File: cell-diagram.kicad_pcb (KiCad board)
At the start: 2 copper layers, 7 parts, among them Q1 Q_NMOS_GSD, Q2 Q_PMOS_GSD, Q3 Q_NMOS_GSD, Q4 Q_PMOS_GSD, Q5 Q_NMOS_GSD, Q6 Q_NMOS_GSD

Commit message: finish routing
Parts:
- added D1: LED, footprints:LED_1206_ReverseMountSquare1.5mm_HandSolder, B.Cu at (170.2, 96.5)
- added D10: LED, footprints:LED_1206_ReverseMountSquare1.5mm_HandSolder, B.Cu at (157.0, 106.7)
- added D11: LED, footprints:LED_1206_ReverseMountSquare1.5mm_HandSolder, B.Cu at (150.4, 102.1)
- added D12: LED, footprints:LED_1206_ReverseMountSquare1.5mm_HandSolder, B.Cu at (150.4, 113.3)
- added D13: LED, footprints:LED_1206_ReverseMountSquare1.5mm_HandSolder, B.Cu at (129.5, 83.8)
- added D14: LED, footprints:LED_1206_ReverseMountSquare1.5mm_HandSolder, B.Cu at (129.5, 101.6)
- added D15: LED, footprints:LED_1206_ReverseMountSquare1.5mm_HandSolder, B.Cu at (129.5, 119.4)
- added D16: LED, footprints:LED_1206_ReverseMountSquare1.5mm_HandSolder, B.Cu at (175.3, 83.8)
- added D17: LED, footprints:LED_1206_ReverseMountSquare1.5mm_HandSolder, B.Cu at (175.3, 101.6)
- added D18: LED, footprints:LED_1206_ReverseMountSquare1.5mm_HandSolder, B.Cu at (175.3, 119.4)
- added D2: LED, footprints:LED_1206_ReverseMountSquare1.5mm_HandSolder, B.Cu at (160.5, 88.9)
- added D3: LED, footprints:LED_1206_ReverseMountSquare1.5mm_HandSolder, B.Cu at (144.3, 88.9)
- added D4: LED, footprints:LED_1206_ReverseMountSquare1.5mm_HandSolder, B.Cu at (134.6, 96.5)
- added D5: LED, footprints:LED_1206_ReverseMountSquare1.5mm_HandSolder, B.Cu at (154.4, 102.1)
- added D6: LED, footprints:LED_1206_ReverseMountSquare1.5mm_HandSolder, B.Cu at (154.4, 113.3)
- added D7: LED, footprints:LED_1206_ReverseMountSquare1.5mm_HandSolder, B.Cu at (147.8, 108.7)
- added D8: LED, footprints:LED_1206_ReverseMountSquare1.5mm_HandSolder, B.Cu at (140.7, 108.7)
- added D9: LED, footprints:LED_1206_ReverseMountSquare1.5mm_HandSolder, B.Cu at (164.1, 106.7)
- added J1: USB_B_Micro, Connector_USB:USB_Micro-B_Wuerth_629105150521, B.Cu at (167.6, 121.9)
- added Q10: Q_NMOS_GSD, Package_TO_SOT_SMD:SOT-23_Handsoldering, B.Cu at (131.1, 113.8)
- added Q11: Q_NMOS_GSD, Package_TO_SOT_SMD:SOT-23_Handsoldering, B.Cu at (173.7, 113.8)
- added Q7: Q_NMOS_GSD, Package_TO_SOT_SMD:SOT-23_Handsoldering, B.Cu at (149.9, 90.4)
- added Q8: Q_NMOS_GSD, Package_TO_SOT_SMD:SOT-23_Handsoldering, B.Cu at (140.7, 112.5)
- added Q9: Q_NMOS_GSD, Package_TO_SOT_SMD:SOT-23_Handsoldering, B.Cu at (164.1, 102.9)
- added R10: R_US, Resistor_SMD:R_0805_2012Metric_Pad1.15x1.40mm_HandSolder, B.Cu at (158.0, 109.7)
- added R11: R_US, Resistor_SMD:R_0805_2012Metric_Pad1.15x1.40mm_HandSolder, B.Cu at (147.3, 102.1)
- added R12: R_US, Resistor_SMD:R_0805_2012Metric_Pad1.15x1.40mm_HandSolder, B.Cu at (147.3, 113.3)
- added R13: R_US, Resistor_SMD:R_0805_2012Metric_Pad1.15x1.40mm_HandSolder, B.Cu at (129.5, 89.4)
- added R14: R_US, Resistor_SMD:R_0805_2012Metric_Pad1.15x1.40mm_HandSolder, B.Cu at (129.5, 107.2)
- added R15: R_US, Resistor_SMD:R_0805_2012Metric_Pad1.15x1.40mm_HandSolder, B.Cu at (129.5, 124.5)
- added R16: R_US, Resistor_SMD:R_0805_2012Metric_Pad1.15x1.40mm_HandSolder, B.Cu at (175.3, 89.4)
- added R17: R_US, Resistor_SMD:R_0805_2012Metric_Pad1.15x1.40mm_HandSolder, B.Cu at (175.3, 107.2)
- added R18: R_US, Resistor_SMD:R_0805_2012Metric_Pad1.15x1.40mm_HandSolder, B.Cu at (175.3, 124.5)
- added R19: 10K, Resistor_SMD:R_0805_2012Metric_Pad1.15x1.40mm_HandSolder, B.Cu at (169.2, 90.9)
- added R2: R_US, Resistor_SMD:R_0805_2012Metric_Pad1.15x1.40mm_HandSolder, B.Cu at (154.9, 88.9)
- added R20: 10K, Resistor_SMD:R_0805_2012Metric_Pad1.15x1.40mm_HandSolder, B.Cu at (160.0, 78.7)
- added R3: R_US, Resistor_SMD:R_0805_2012Metric_Pad1.15x1.40mm_HandSolder, B.Cu at (138.7, 88.9)
- added R4: R_US, Resistor_SMD:R_0805_2012Metric_Pad1.15x1.40mm_HandSolder, B.Cu at (137.7, 96.5)
- added R5: R_US, Resistor_SMD:R_0805_2012Metric_Pad1.15x1.40mm_HandSolder, B.Cu at (157.5, 102.1)
- added R6: R_US, Resistor_SMD:R_0805_2012Metric_Pad1.15x1.40mm_HandSolder, B.Cu at (157.5, 113.3)
- added R7: R_US, Resistor_SMD:R_0805_2012Metric_Pad1.15x1.40mm_HandSolder, B.Cu at (146.8, 105.7)
- added R8: R_US, Resistor_SMD:R_0805_2012Metric_Pad1.15x1.40mm_HandSolder, B.Cu at (140.7, 105.7)
- added R9: R_US, Resistor_SMD:R_0805_2012Metric_Pad1.15x1.40mm_HandSolder, B.Cu at (164.1, 109.7)
- added REF**: MountingHole_3.2mm_M3_DIN965_Pad, MountingHole:MountingHole_3.2mm_M3_DIN965_Pad, F.Cu at (135.6, 80.3)
- added SW1: SW_Write, Button_Switch_THT:SW_PUSH_6mm, F.Cu at (167.1, 85.9)
- added SW2: SW_Input, footprints:Switch_DPDT_THT_CK, F.Cu at (144.8, 83.8)
- added SW3: SW_Enable, footprints:Switch_DPDT_THT_CK, F.Cu at (160.0, 83.8)
- added U1: MC74VHC1G125, Package_TO_SOT_SMD:SOT-23-5, B.Cu at (152.4, 84.8)
- added U2: MC74VHC1G125, Package_TO_SOT_SMD:SOT-23-5, B.Cu at (152.4, 79.8)
- Q1: value Q_NMOS_GSD -> Q_PMOS_GSD
- Q4: value Q_PMOS_GSD -> Q_NMOS_GSD
- R1: moved to B.Cu
- moved Q5 58.6 mm to (134.6, 110.2), turned to 90 degrees
- moved Q4 52.9 mm to (162.1, 114.9), turned to 180 degrees
- moved R1 45.8 mm to (167.1, 96.5), turned to 90 degrees
- moved Q6 45.0 mm to (170.2, 108.2), turned to 90 degrees
- moved Q3 41.7 mm to (142.7, 114.8)
- moved Q2 34.7 mm to (162.1, 100.6), turned to 180 degrees
- moved Q1 30.8 mm to (142.7, 100.6)
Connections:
- Q1 pad 1: Net-(Q1-Pad1) -> Internal_R
- Q1 pad 2: (no net) -> VCC
- Q1 pad 3: Net-(Q1-Pad3) -> Internal_L
- Q2 pad 1: Net-(Q2-Pad1) -> Internal_L
- Q2 pad 2: VDD -> VCC
- Q2 pad 3: Net-(Q1-Pad3) -> Internal_R
- Q3 pad 1: Net-(Q2-Pad1) -> Internal_R
- Q3 pad 2: Net-(Q1-Pad3) -> GND
- Q3 pad 3: GND -> Internal_L
- Q4 pad 1: Net-(Q1-Pad3) -> Internal_L
- Q4 pad 2: Net-(Q2-Pad1) -> GND
- Q4 pad 3: VDD -> Internal_R
- Q5 pad 1: Net-(Q1-Pad3) -> Enable
- Q5 pad 2: GND -> External_L
- Q5 pad 3: Net-(Q2-Pad1) -> Internal_L
- Q6 pad 1: Net-(Q1-Pad1) -> Enable
- Q6 pad 2: Net-(Q2-Pad1) -> External_R
- Q6 pad 3: (no net) -> Internal_R
- R1 pad 1: Net-(Q1-Pad1) -> Net-(D1-Pad1)
- R1 pad 2: GND -> Net-(Q7-Pad3)
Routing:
- net VCC: track 0.00 -> 283.0 mm, vias 0 -> 5
- net Enable: track 0.00 -> 98.4 mm, vias 0 -> 1
- net Internal_L: track 0.00 -> 66.1 mm, vias 0 -> 1
- net Internal_R: track 0.00 -> 65.5 mm, vias 0 -> 1
- net Net-(Q8-Pad3): track 0.00 -> 56.4 mm
- net Net-(R19-Pad2): track 0.00 -> 55.9 mm
- net Net-(Q9-Pad3): track 0.00 -> 54.4 mm
- net External_L: track 0.00 -> 49.6 mm, vias 0 -> 2
- net External_R: track 0.00 -> 47.1 mm, vias 0 -> 2
- net Net-(Q7-Pad3): track 0.00 -> 41.4 mm
- net Net-(Q11-Pad3): track 0.00 -> 38.9 mm
- net Net-(Q10-Pad3): track 0.00 -> 38.4 mm
- net GND: track 0.00 -> 25.8 mm, vias 0 -> 8
- net Net-(J1-Pad6): track 0.00 -> 15.2 mm
- net Net-(SW2-Pad2): track 0.00 -> 7.71 mm
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- added copper zone on B.Cu, net GND
- added copper zone on F.Cu, net GND
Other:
- board outline added: 50.8 x 50.8 mm
- board text added: "S-RAM Cell"

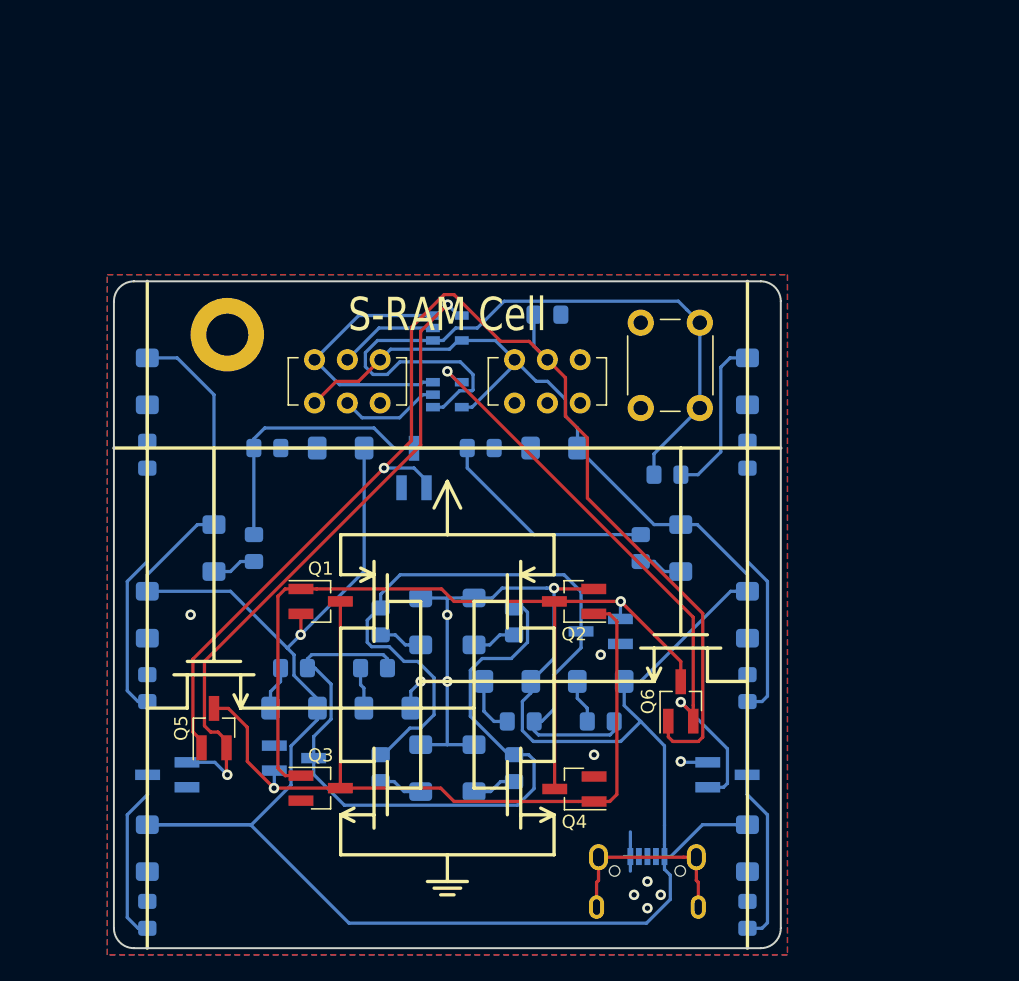
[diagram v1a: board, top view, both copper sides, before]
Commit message: add optional power regulation
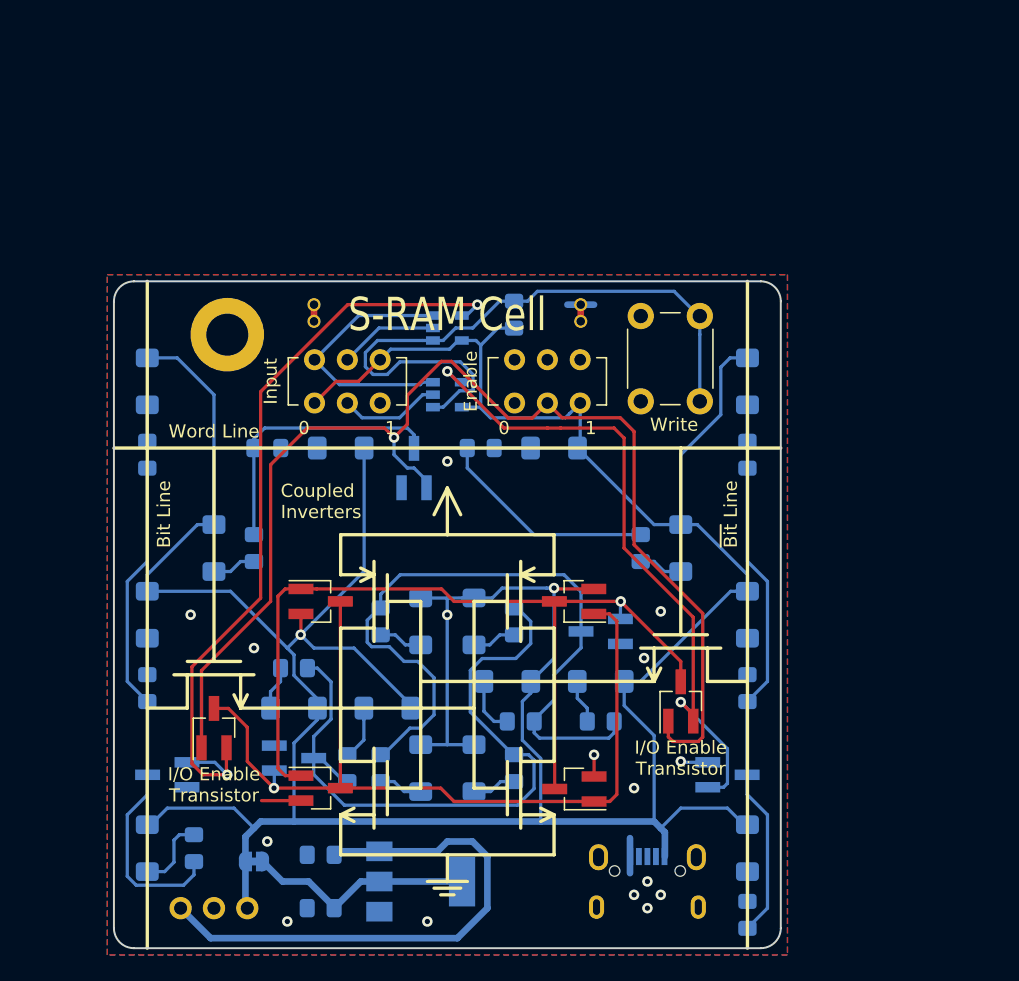
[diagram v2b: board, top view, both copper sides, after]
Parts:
- removed R20: 10K, Resistor_SMD:R_0805_2012Metric_Pad1.15x1.40mm_HandSolder
- added C1: C, Capacitor_SMD:C_0805_2012Metric_Pad1.15x1.40mm_HandSolder, B.Cu at (142.7, 119.9)
- added C2: C, Capacitor_SMD:C_0805_2012Metric_Pad1.15x1.40mm_HandSolder, B.Cu at (142.7, 124.0)
- added J2: Conn_01x03, #footprints:PowerHeader_P2.54mm, B.Cu at (137.2, 124.0)
- added JP1: Regulator_Enable, Jumper:SolderJumper-2_P1.3mm_Bridged_RoundedPad1.0x1.5mm, B.Cu at (137.7, 120.4)
- added REF**: SnakeBite_P1.27mm, #footprints:SnakeBite_P1.27mm, F.Cu at (162.6, 78.0)
- added REF**: SnakeBite_P1.27mm, #footprints:SnakeBite_P1.27mm, F.Cu at (142.2, 78.0)
- added U3: LD1117S50TR, Package_TO_SOT_SMD:SOT-223-3_TabPin2, B.Cu at (150.4, 121.9)
- SW3: footprint footprints:Switch_DPDT_THT_CK -> #footprints:Switch_DPDT_THT_CK
- moved R19 16.9 mm to (157.5, 78.7), turned to 90 degrees
- moved R7 7.89 mm to (144.8, 113.3), turned to 270 degrees
- moved R15 6.20 mm to (133.1, 119.4)
- moved SW1 0.51 mm to (167.1, 85.3)
- turned SW3 to 180 degrees
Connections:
- SW3 pad 3: (no net) -> GND
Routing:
- net /Raw: track 0.00 -> 41.8 mm
- net /Regulated: track 0.00 -> 17.6 mm
- net Net-(J1-Pad6): track 15.2 -> 0.00 mm
- net External_L: track 49.6 -> 60.0 mm
- net GND: track 25.8 -> 34.3 mm, vias 8 -> 15
- net Net-(R19-Pad2): track 55.9 -> 49.8 mm
- net External_R: track 47.1 -> 52.0 mm
- net Net-(Q8-Pad3): track 56.4 -> 52.0 mm
- net Enable: track 98.4 -> 94.4 mm
- net Net-(D15-Pad1): track 2.27 -> 5.71 mm
- net VCC: track 283.0 -> 280.8 mm, vias 5 -> 3
- net Net-(Q11-Pad3): track 38.9 -> 37.6 mm
- net Net-(Q10-Pad3): track 38.4 -> 39.7 mm
- net Net-(D7-Pad1): track 3.15 -> 4.15 mm
- net Net-(Q7-Pad3): track 41.4 -> 42.0 mm
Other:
- net class Power added: clearance 0.2, trace_width 0.508, via_dia 0.8, via_drill 0.4
- board text added: "0"
- board text added: "1"
- board text added: "Bit Line"
- board text added: "Coupled Inverters"
- board text added: "Enable"
- board text added: "I/O Enable Transistor"
- board text added: "Input"
- board text added: "VCC GND RAW"
- board text added: "Word Line"
- board text added: "Write"
- board text added: "~Bit Line"

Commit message: make some cosmetic improvements
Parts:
- added REF**: TY_Mark_6mm_Copper, #footprints:TY_Mark_6mm_Copper, B.Cu at (141.7, 95.5)
- added REF**: OSHW-Symbol_6.7x6mm_Copper, Symbol:OSHW-Symbol_6.7x6mm_Copper, B.Cu at (159.5, 120.9)
- D1, D10, D11, D12, D13, D14, D15, D16, D17, D18, D2, D3, D4, D5, D6, D7, D8, D9: value LED -> (none); footprint footprints:LED_1206_ReverseMountSquare1.5mm_HandSolder -> #footprints:LED_1206_ReverseMountSquare1.5mm_HandSolder
- J1: footprint Connector_USB:USB_Micro-B_Wuerth_629105150521 -> Connector_USB:USB_Micro-B_Molex-105017-0001
- J2: value Conn_01x03 -> PowerHeader
- Q1, Q2: value Q_PMOS_GSD -> PMOS_GSD
- Q10, Q11, Q3, Q4, Q5, Q6, Q7, Q8, Q9: value Q_NMOS_GSD -> NMOS_GSD
- R1, R10, R11, R12, R13, R14, R15, R16, R17, R18, R2, R3, R4, R5, R6, R7, R8, R9: value R_US -> (none)
- REF** (x2): value SnakeBite_P1.27mm -> Mounting Holes
- REF**: value MountingHole_3.2mm_M3_DIN965_Pad -> 4-40 Mount
- SW2: footprint footprints:Switch_DPDT_THT_CK -> #footprints:Switch_DPDT_THT_CK
- moved R7 7.89 mm to (146.8, 105.7), turned to 180 degrees
- moved J1 2.41 mm to (167.6, 124.3)
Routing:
- net Net-(J1-Pad6): track 0.00 -> 12.0 mm
- net VCC: track 280.8 -> 291.5 mm
- net Enable: track 94.4 -> 92.7 mm
- net External_R: track 52.0 -> 50.4 mm
- net GND: track 34.3 -> 34.7 mm, vias 15 -> 13
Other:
- board text added: "Tobin Yehle v1 2020-06"
- board text added: "github.com/tyehle/sram-cell"
